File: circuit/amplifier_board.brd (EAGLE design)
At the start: 60 x 30 mm, 25 parts

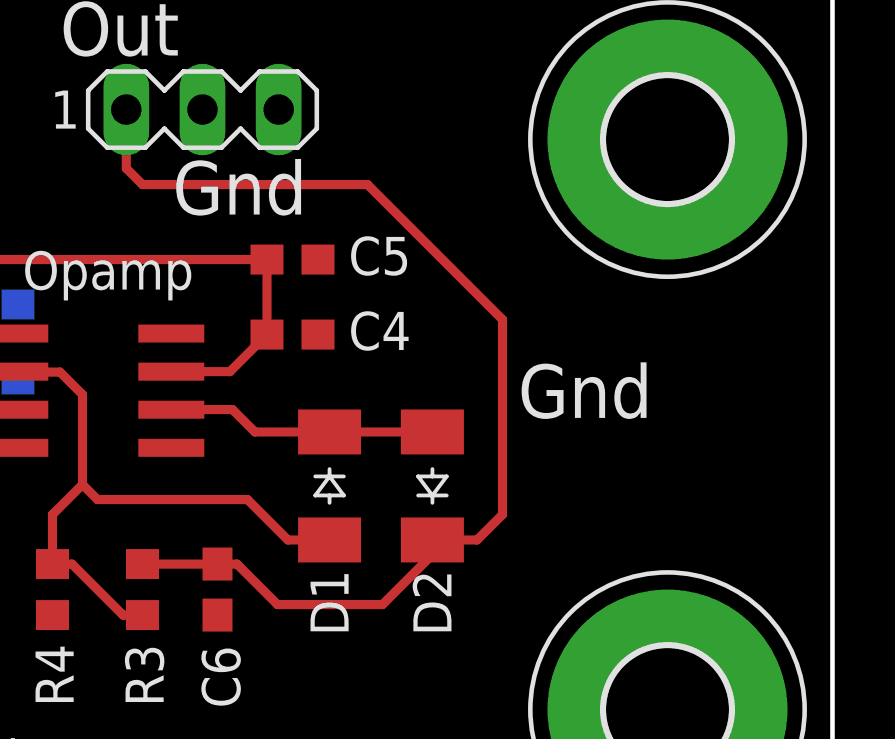
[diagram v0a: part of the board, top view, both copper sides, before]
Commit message: boards: Increased trace width so Jim can actually mill the boards.
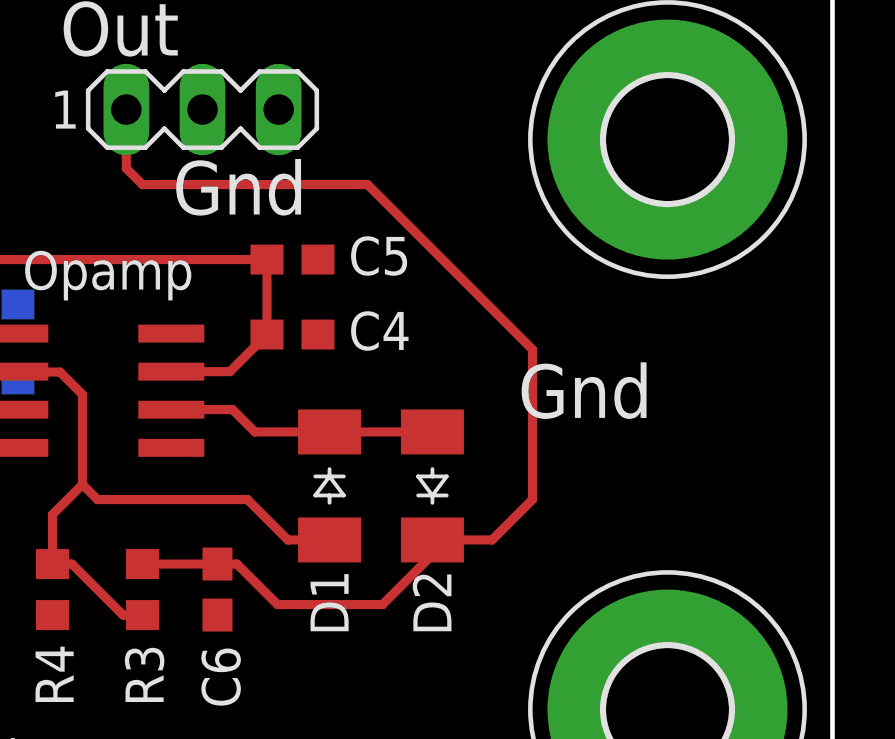
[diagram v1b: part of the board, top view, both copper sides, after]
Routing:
- net DIG_READOUT: track 37.2 -> 37.8 mm
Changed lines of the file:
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@@
 <classes>
 <class number="0" name="default" width="0.3048" drill="0">
-<clearance class="0" value="0.3048"/>
+<clearance class="0" value="0.508"/>
 </class>
 <class number="1" name="high_freq" width="3" drill="0">
@@
 <contactref element="D2" pad="C"/>
 <wire x1="45" y1="9" x2="46.664" y2="10.664" width="0.3048" layer="1"/>
-<wire x1="46.664" y1="10.664" x2="46.664" y2="11.154" width="0.3048" layer="1"/>
 <contactref element="R3" pad="2"/>
 <contactref element="C6" pad="1"/>
@@
 <wire x1="36.46" y1="23.54" x2="37" y2="23" width="0.3048" layer="1"/>
 <wire x1="37" y1="23" x2="44.5" y2="23" width="0.3048" layer="1"/>
-<wire x1="44.5" y1="23" x2="49" y2="18.5" width="0.3048" layer="1"/>
-<wire x1="49" y1="18.5" x2="49" y2="12" width="0.3048" layer="1"/>
-<wire x1="49" y1="12" x2="48.154" y2="11.154" width="0.3048" layer="1"/>
-<wire x1="48.154" y1="11.154" x2="46.664" y2="11.154" width="0.3048" layer="1"/>
+<wire x1="44.5" y1="23" x2="50" y2="17.5" width="0.3048" layer="1"/>
+<wire x1="48.654" y1="11.154" x2="46.664" y2="11.154" width="0.3048" layer="1"/>
+<wire x1="50" y1="17.5" x2="50" y2="12.5" width="0.3048" layer="1"/>
+<wire x1="50" y1="12.5" x2="48.654" y2="11.154" width="0.3048" layer="1"/>
+<wire x1="46.664" y1="10.664" x2="46.664" y2="11.154" width="0" layer="19" extent="1-1"/>
 </signal>
 <signal name="OUT_2">
